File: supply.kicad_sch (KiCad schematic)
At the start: 24 parts

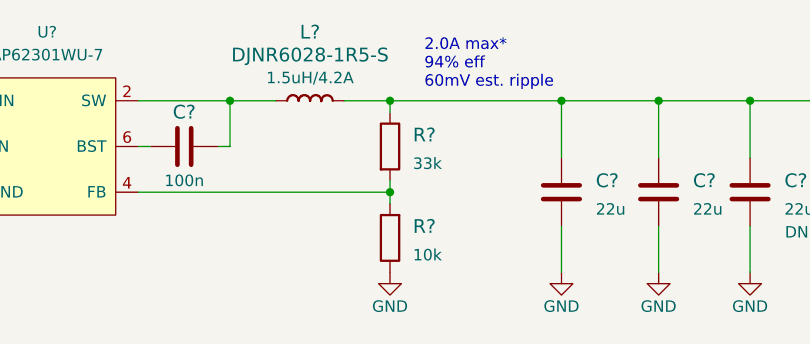
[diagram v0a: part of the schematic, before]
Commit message: Redesigned 3.3V supply taking into the consideration reduced power requirements
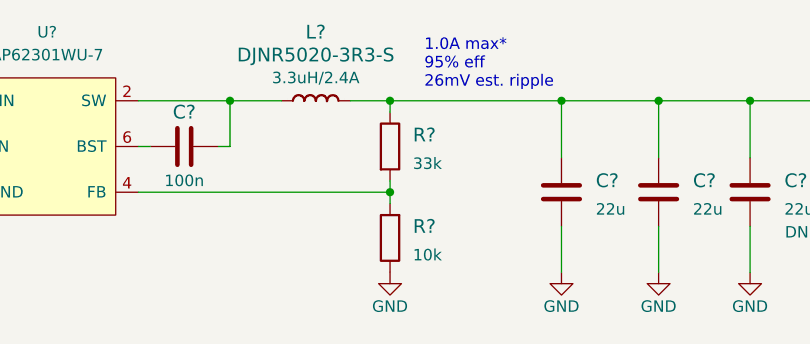
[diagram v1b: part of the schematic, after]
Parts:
- removed L?: DJNR6028-1R5-S, crosslink-nx-video-converter:L_6x6mm-, symbol crosslink-nx-video-converter:DJNR6028-1R5-S
- added L?: DJNR5020-3R3-S, crosslink-nx-video-converter:L_4.9x4.9mm, symbol crosslink-nx-video-converter:DJNR5020-3R3-S
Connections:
- net at C?.1, C?.1, C?.1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: now also L?.2 (P)
- net at C?.2, U?.2 (SW): now also L?.1 (P)
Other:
- note added: "1.0A max* 95% eff 26mV est. ripple"
- note removed: "2.0A max* 94% eff 60mV est. ripple"

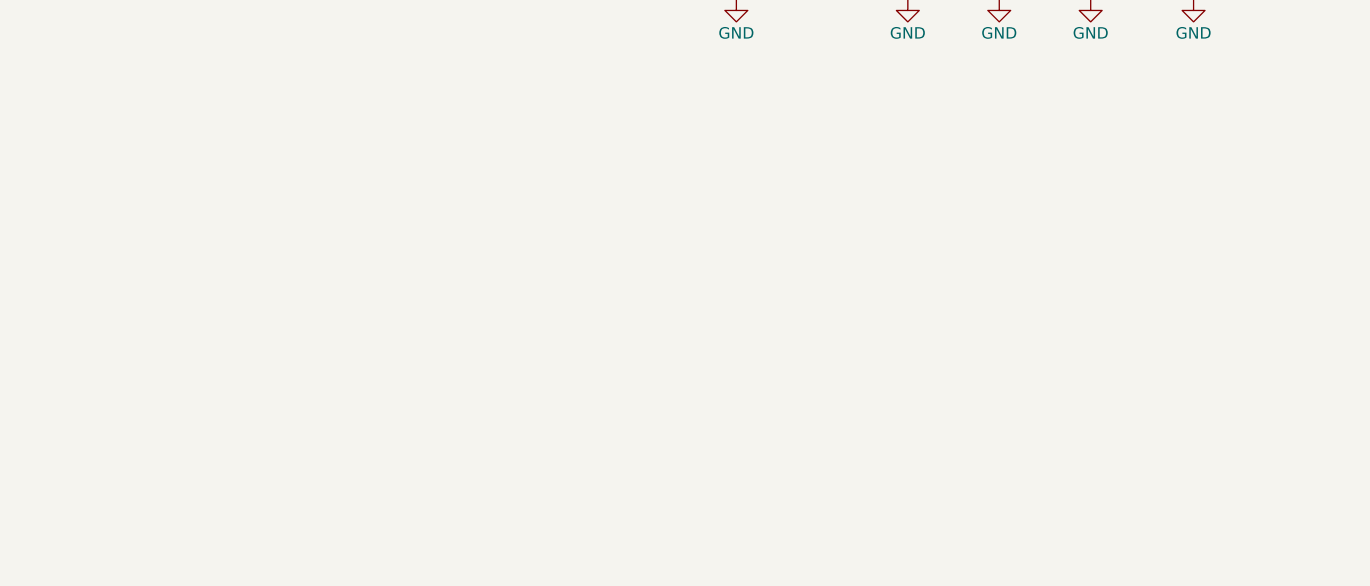
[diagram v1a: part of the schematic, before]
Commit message: Added DRAM SMPS
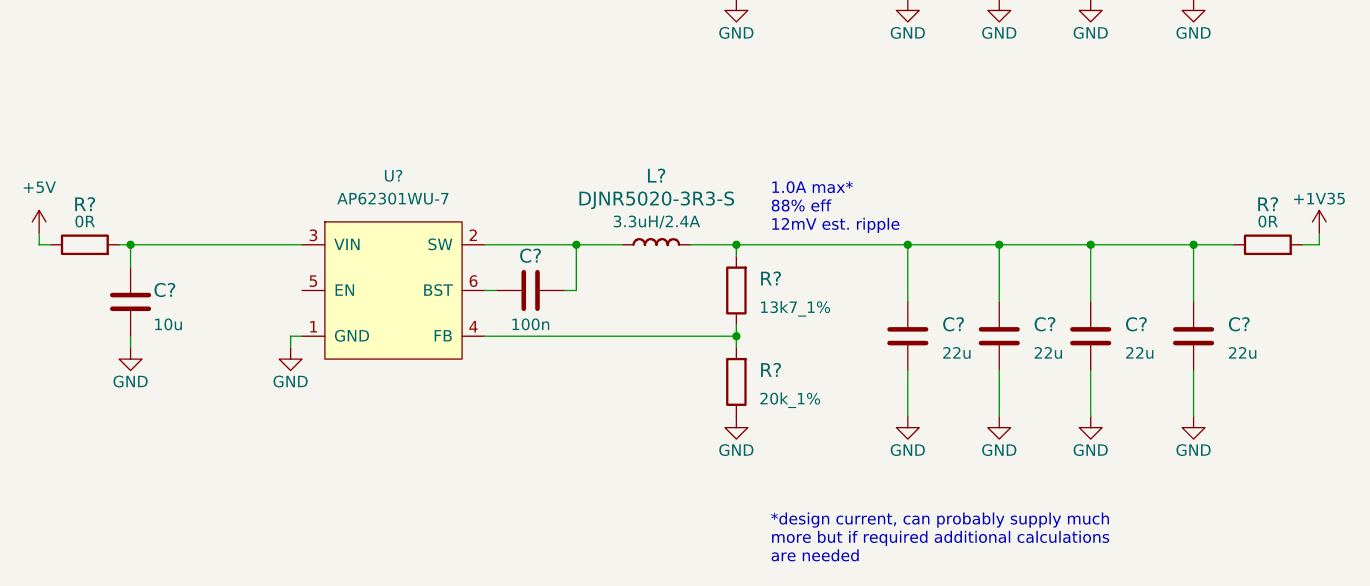
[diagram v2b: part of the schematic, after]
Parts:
- added C?: C_100n_0603, antmicro-footprints:0603-cap, symbol antmicroCapacitors0603:C_100n_0603
- added C? (x4): C_22u_0805, antmicro-footprints:0805-cap, symbol antmicroCapacitorsmisc:C_22u_0805
- added C?: C_10u_0603, antmicro-footprints:0603-cap, symbol antmicroCapacitors0603:C_10u_0603
- added L?: DJNR5020-3R3-S, crosslink-nx-video-converter:L_4.9x4.9mm, symbol crosslink-nx-video-converter:DJNR5020-3R3-S
- added R?: R_20k_1%_0603, antmicro-footprints:0603-res, symbol antmicroResistors0603:R_20k_1%_0603
- added R? (x2): R_0R_0805, antmicro-footprints:0805-res, symbol antmicroResistorsmisc:R_0R_0805
- added R?: R_13k7_1%_0603, antmicro-footprints:0603-res, symbol antmicroResistors0603:R_13k7_1%_0603
- added U?: AP62301WU-7, antmicro-footprints:TSOT23-6, symbol antmicroDCDCConverters:AP62301WU-7
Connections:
- net +5V: now also R?.1
- net GND: now also C?.2, C?.2, C?.2, C?.2, C?.2, R?.1, U?.1 (GND)
- new net: R?.1, R?.2, U?.4 (FB)
- new net: C?.1, U?.6 (BST)
- new net: C?.2, L?.1 (P), U?.2 (SW)
- new net: C?.1, C?.1, C?.1, C?.1, L?.2 (P), R?.1, R?.2
- new net: C?.1, R?.2, U?.3 (VIN)
- new net +1V35: R?.2
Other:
- note added: "*design current, can probably supply much more but if required additional calculations are needed"
- note added: "1.0A max* 88% eff 12mV est. ripple"

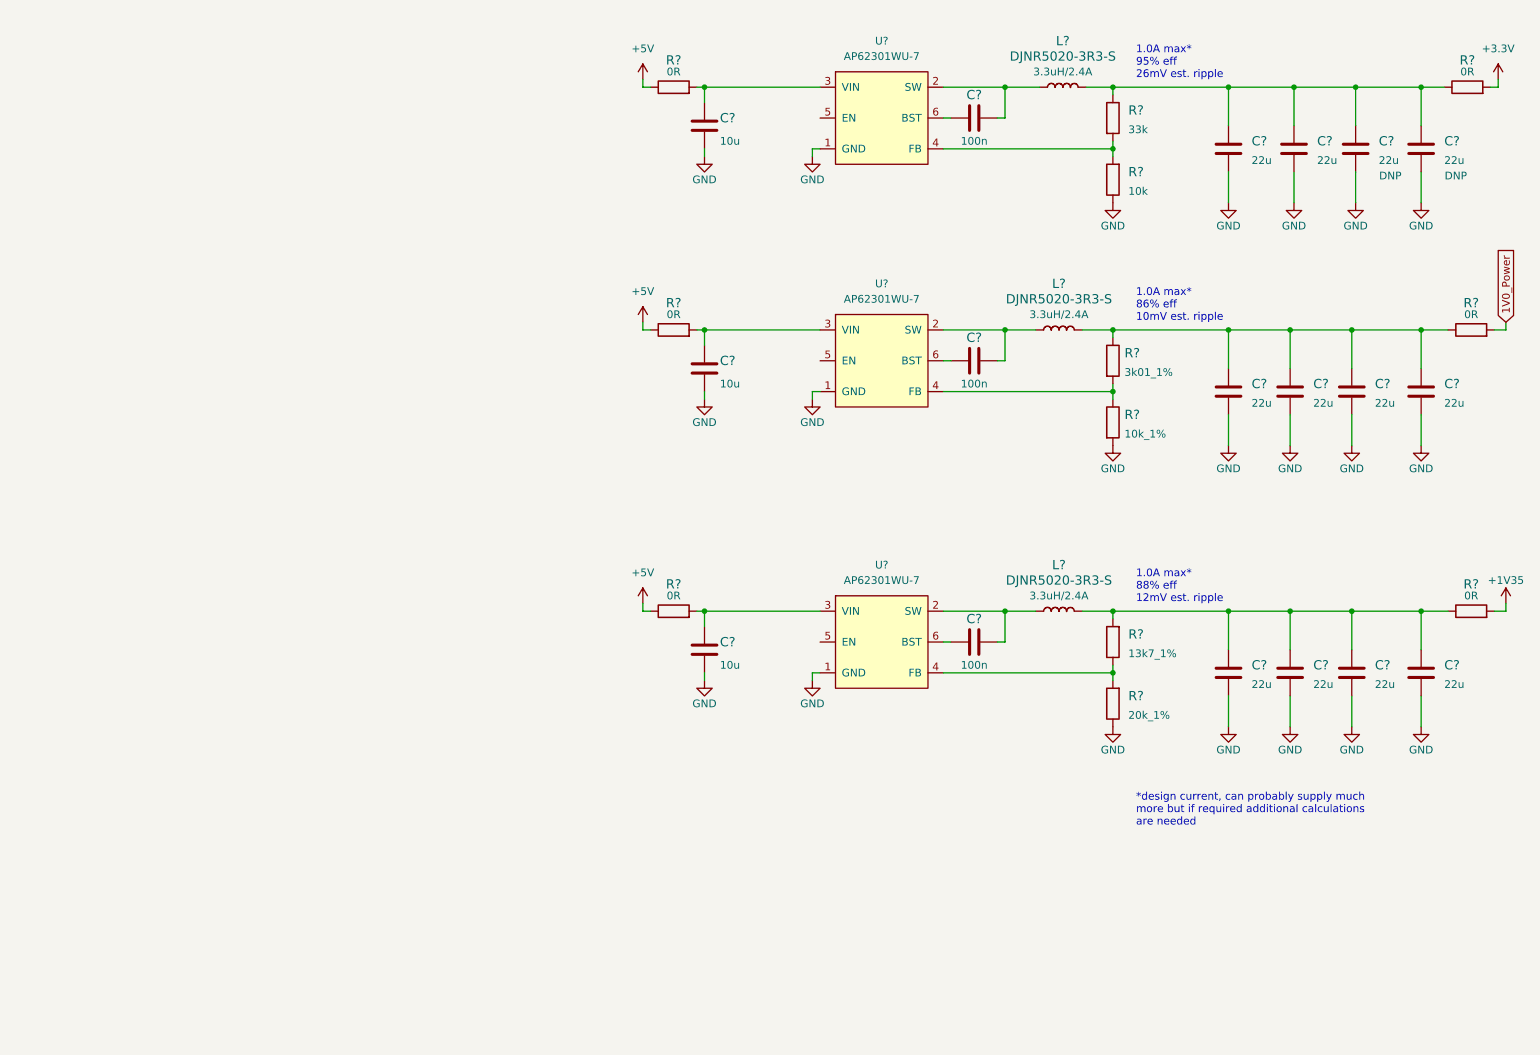
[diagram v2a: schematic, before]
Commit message: Added LDOs
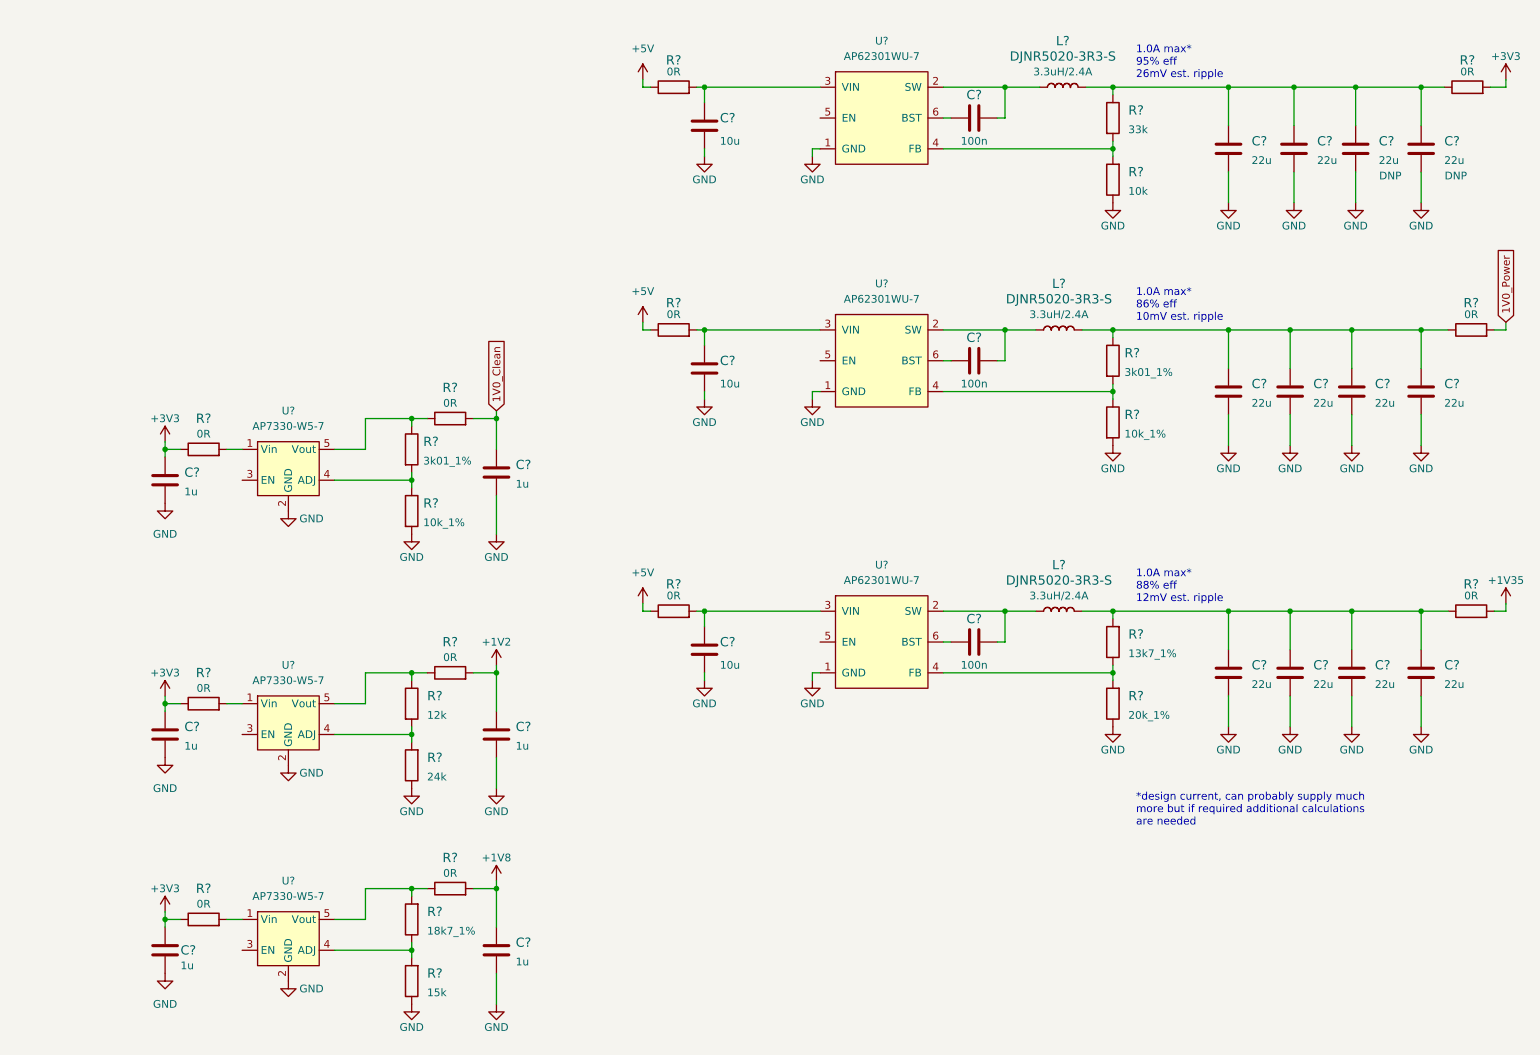
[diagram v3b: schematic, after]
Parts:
- added C? (x6): C_1u_0603, antmicro-footprints:0603-cap, symbol antmicroCapacitors0603:C_1u_0603
- added R?: R_18k7_1%_0603, antmicro-footprints:0603-res, symbol antmicroResistors0603:R_18k7_1%_0603
- added R?: R_12k_0603, antmicro-footprints:0603-res, symbol antmicroResistors0603:R_12k_0603
- added R?: R_24k_0603, antmicro-footprints:0603-res, symbol antmicroResistors0603:R_24k_0603
- added R? (x6): R_0R_0603, antmicro-footprints:0603-res, symbol antmicroResistors0603:R_0R_0603
- added R?: R_3k01_1%_0603, antmicro-footprints:0603-res, symbol crosslink-nx-video-converter:R_3k01_1%_0603
- added R?: R_15k_0603, antmicro-footprints:0603-res, symbol antmicroResistors0603:R_15k_0603
- added R?: R_10k_1%_0603, antmicro-footprints:0603-res, symbol crosslink-nx-video-converter:R_10k_1%_0603
- added U? (x3): AP7330-W5-7, antmicro-footprints:SOT-23-5, symbol antmicroPMICVoltageRegulatorsLinear:AP7330-W5-7
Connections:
- net +3V3: now also C?.1, C?.1, C?.1, R?.1, R?.1, R?.1
- net GND: now also C?.2, C?.2, C?.2, C?.2, C?.2, C?.2, R?.1, R?.1, R?.2, U?.2 (GND), U?.2 (GND), U?.2 (GND)
- new net: R?.1, R?.2, U?.4 (ADJ) (x2)
- new net: R?.1, R?.2, U?.5 (Vout)
- new net: R?.2, U?.1 (Vin) (x3)
- new net: R?.1, R?.1, U?.5 (Vout) (x2)
- new net: R?.2, R?.2, U?.4 (ADJ)
- new net +1V2: C?.1, R?.2
- new net +1V8: C?.1, R?.2
- new net 1V0_Clean: C?.1, R?.2

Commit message: Completed schematic of MT41K128M16JT memory module
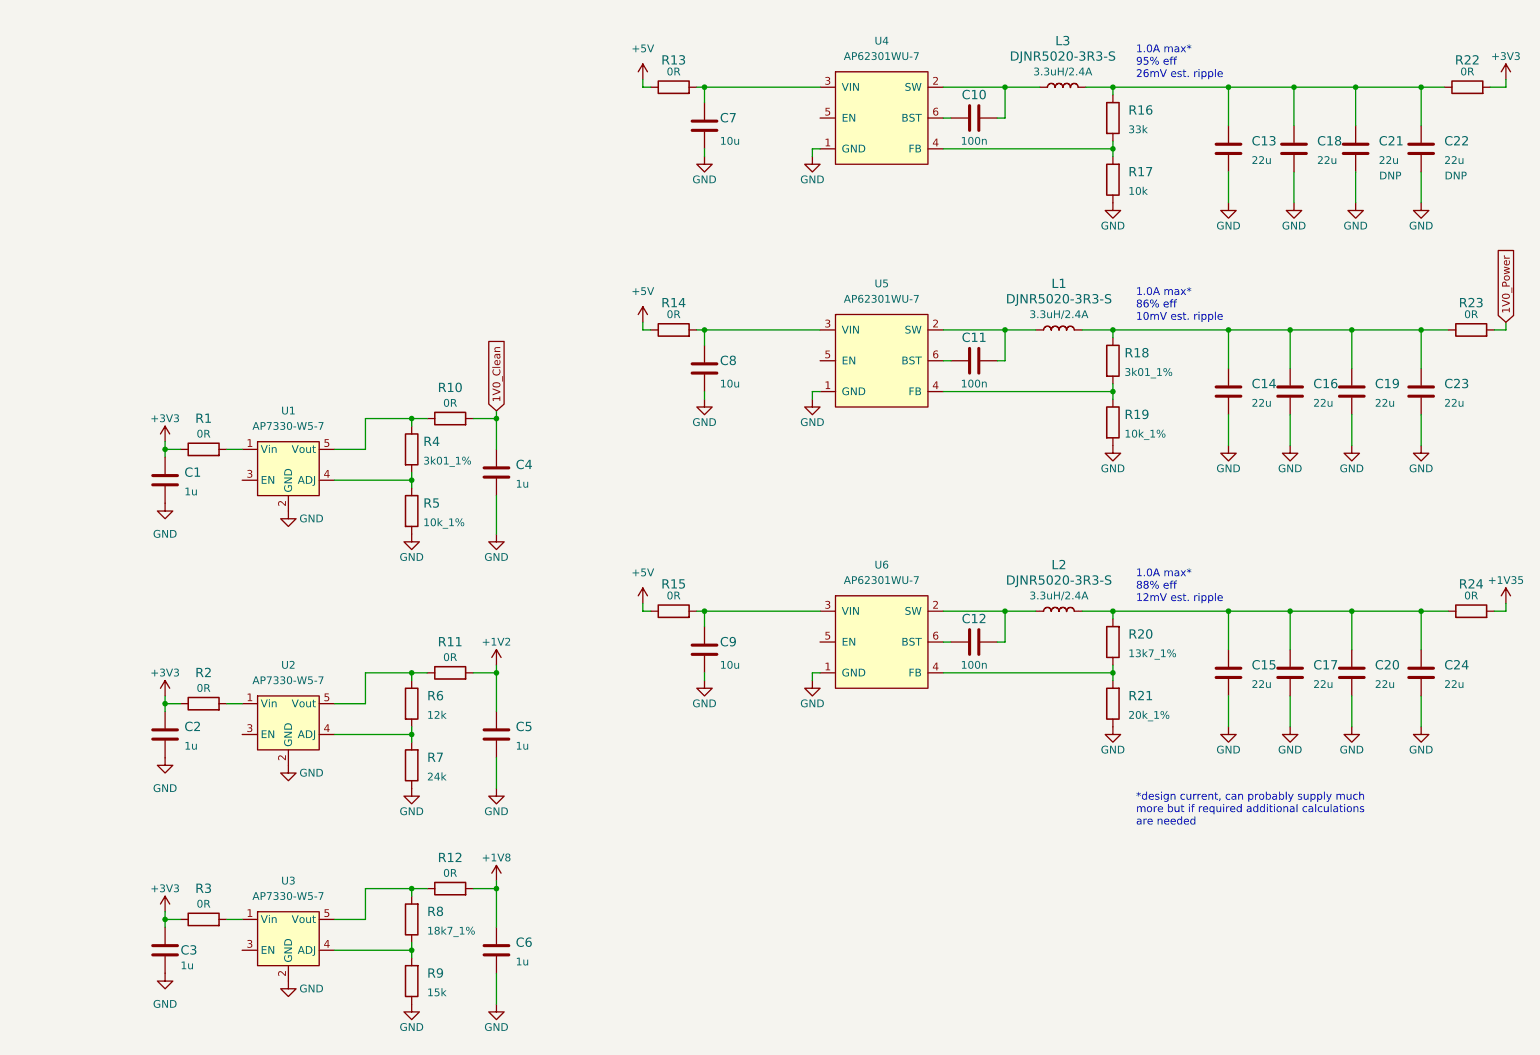
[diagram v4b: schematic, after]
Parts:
- gave numbers to parts that had none: 57
